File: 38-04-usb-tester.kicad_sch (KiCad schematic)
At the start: 64 parts, among them J1 Conn_1x05, J2 USB_C_12401832E402A, J3 USB_C_12401832E402A, J4 USB_Micro-B_KH-MICRO5P-JN, J5 USB_Mini-B_U-M-M5DD-W-1, J6 USB3_A_HC-USB3.0-L168-WP, SW1 SW_DPDT_x2, SW2 ZX-1.27BM-4PSMD, U1 STM32C031K6Tx

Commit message: edited schematic, added solder mask expansion, added more thermal reliefs
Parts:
- BT1, C3, C5, J1, R1, R2, R3, R4, R5, SW1: LCSC Part # (none) -> DNP; now not fitted
- C1, C2, C4: LCSC Part # (none) -> C527030
- D1, D10, D11, D12, D13, D14, D15, D16, D17, D18, D19, D2, D20, D21, D22, D23, D24, D25, D3, D4, D5, D6, D7, D8, D9: LCSC Part # (none) -> C91839
- H1, H10, H11, H12, H2, H3, H4, H5, H6, H7, H8, H9: LCSC Part # (none) -> DNP
- J2, J3: LCSC Part # (none) -> C464604
- J4: LCSC Part # (none) -> C962222
- J5: LCSC Part # (none) -> C145778
- J6: LCSC Part # (none) -> C7501850
- RN1, RN2, RN3, RN4, RN5, RN6, RN7: LCSC Part # (none) -> C136833
- SW2: LCSC Part # (none) -> C5160896
- U1: value STM32C031K6Tx -> STM32C031K6T6; JLPCB_MPN (none) -> STM32C031K6T6; JLPCB_Mfg (none) -> STMicroelectronics; JLPCB_Part_No (none) -> C5456169; JLPCB_Price (none) -> $1.2900; JLPCB_URL (none) -> https://jlcpcb.com/partdetail/Stmicroelectronics-STM32C031K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; LCSC Part # (none) -> C5456169

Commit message: rev 1 sent for prod
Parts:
- C1, C2, C4: Basic/Extended (none) -> B; JLPCB_MPN CC0402MRY5V6BB104 -> CL05B104KO5NNNC; JLPCB_Mfg YAGEO -> Samsung Electro-Mechanics; JLPCB_Part_No C527030 -> C1525; JLPCB_Price $0.0016 -> $0.0009; JLPCB_URL (none) -> https://jlcpcb.com/partdetail/1877-CL05B104KO5NNNC/C1525; LCSC Part # C527030 -> C1525
- C3: Basic/Extended (none) -> B; JLPCB_MPN DNP -> CL21A475KAQNNNE; JLPCB_Mfg DNP -> Samsung Electro-Mechanics; JLPCB_Part_No DNP -> C1779; JLPCB_Price DNP -> $0.0110; JLPCB_URL (none) -> https://jlcpcb.com/parts/2nd/Capacitors/Multilayer_Ceramic_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; LCSC Part # DNP -> C1779; now fitted
- C5: Basic/Extended (none) -> B; JLPCB_MPN DNP -> CL21B105KBFNNNE; JLPCB_Mfg DNP -> Samsung Electro-Mechanics; JLPCB_Part_No DNP -> C28323; JLPCB_Price DNP -> $0.0083; JLPCB_URL (none) -> https://jlcpcb.com/partdetail/29074-CL21B105KBFNNNE/C28323; LCSC Part # DNP -> C28323; now fitted
- D1, D10, D11, D12, D13, D14, D15, D16, D17, D18, D19, D2, D20, D21, D22, D23, D24, D25, D3, D4, D5, D6, D7, D8, D9: Basic/Extended (none) -> B; JLPCB_MPN 17-21UYC/S530-A3/TR8 -> KT-0805Y; JLPCB_Mfg Everlight Elec -> Hubei KENTO Elec; JLPCB_Part_No C91839 -> C2296; JLPCB_Price $0.0218 -> $0.0114; JLPCB_URL https://jlcpcb.com/parts/2nd/Optocoupler_LED_Digital_Tube_P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 -> https://jlcpcb.com/partdetail/Hubei_KentoElec-KT0805Y/C2296; LCSC Part # C91839 -> C2296
- J2, J3, J4, J5, J6: Basic/Extended (none) -> E
- R1, R2, R3: Basic/Extended (none) -> B; JLPCB_MPN DNP -> 0805W8F1002T5E; JLPCB_Mfg DNP -> UNI-ROYAL(Uniroyal Elec); JLPCB_Part_No DNP -> C17414; JLPCB_Price DNP -> (none); JLPCB_URL (none) -> https://jlcpcb.com/partdetail/18102-0805W8F1002T5E/C17414; LCSC Part # DNP -> C17414; now fitted
- R4: value 1K -> 2K; Basic/Extended (none) -> B; JLPCB_MPN DNP -> 0805W8F2001T5E; JLPCB_Mfg DNP -> UNI-ROYAL(Uniroyal Elec); JLPCB_Part_No DNP -> C17604; JLPCB_Price DNP -> (none); JLPCB_URL (none) -> https://jlcpcb.com/partdetail/18292-0805W8F2001T5E/C17604; LCSC Part # DNP -> C17604; now fitted
- R5: Basic/Extended (none) -> B; JLPCB_MPN DNP -> 0805W8F2001T5E; JLPCB_Mfg DNP -> UNI-ROYAL(Uniroyal Elec); JLPCB_Part_No DNP -> C17604; JLPCB_Price DNP -> (none); JLPCB_URL (none) -> https://jlcpcb.com/partdetail/18292-0805W8F2001T5E/C17604; LCSC Part # DNP -> C17604; now fitted
- RN1, RN2, RN3, RN4, RN5, RN6, RN7: value 1K -> 1K6; Basic/Extended (none) -> E; JLPCB_MPN YC164-JR-071K1L -> YC124-FR-071K6L; JLPCB_Part_No C136833 -> C728711; JLPCB_Price $0.007 -> $0.0024; LCSC Part # C136833 -> C728711
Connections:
- no-connect marks 18 -> 19

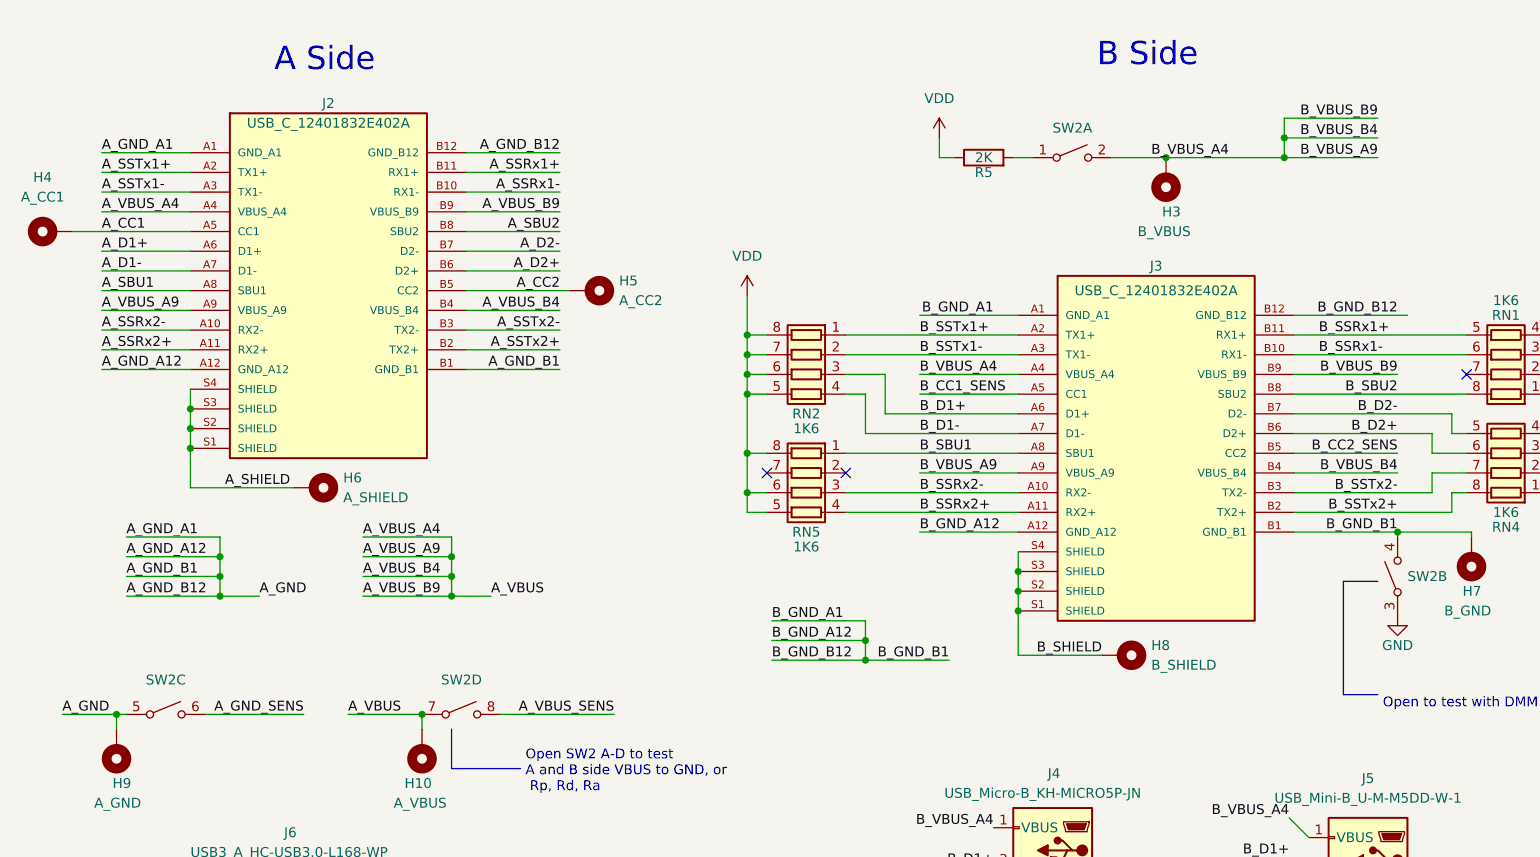
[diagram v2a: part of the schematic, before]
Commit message: correct SW2 footprint and symbol pin numbering
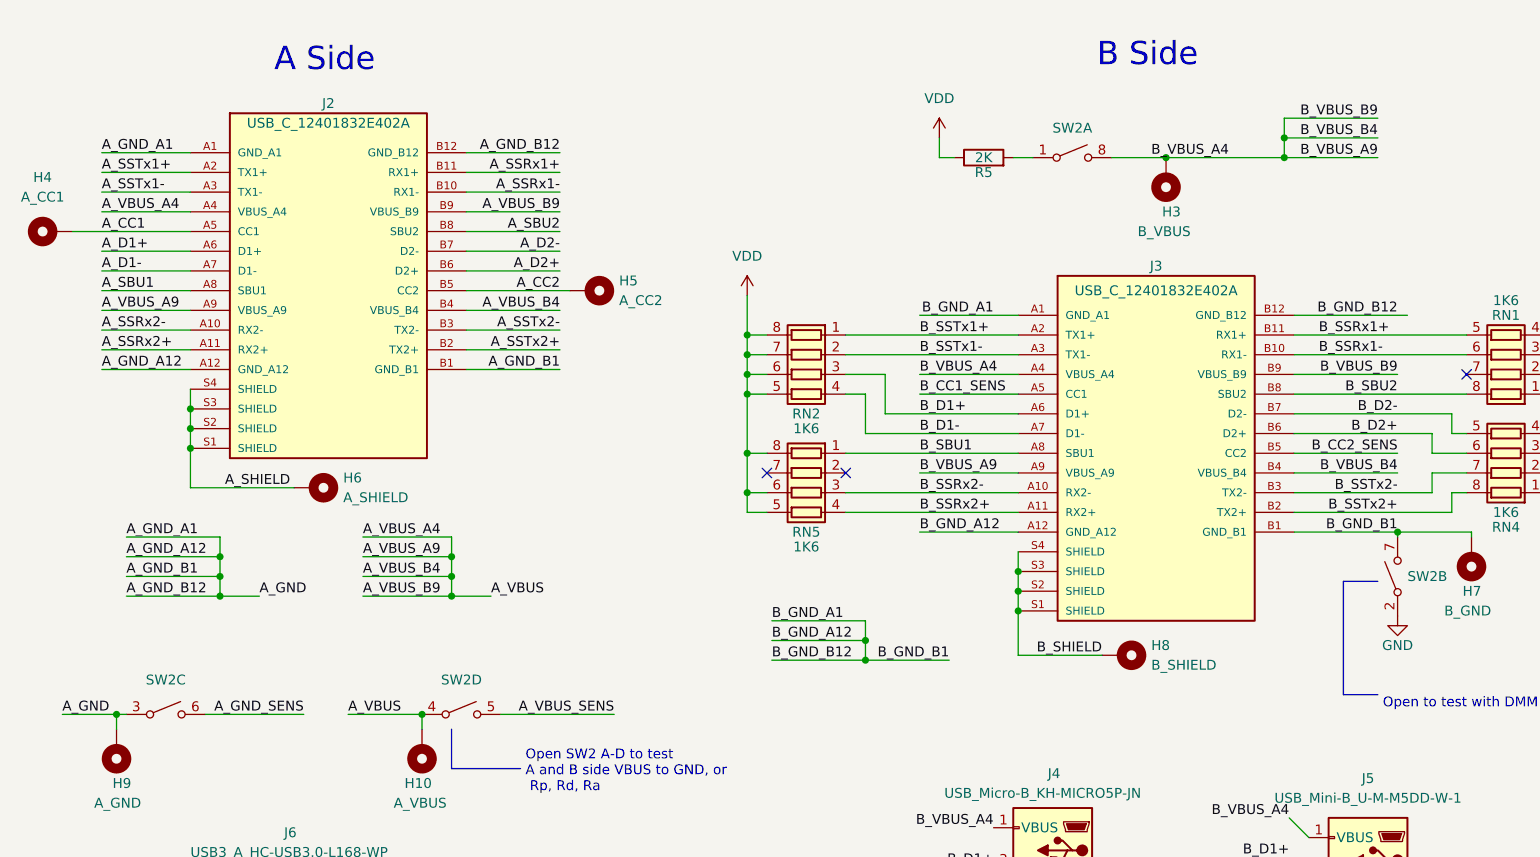
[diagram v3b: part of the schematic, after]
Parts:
- SW2: symbol 01B-UserSchematics:SW_DIP_x04_Separated -> 02-UserSymbols:SW_DIP_x04_Separated
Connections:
- net A_GND: now also SW2.3; no longer SW2.5
- net A_VBUS: now also SW2.4; no longer SW2.7
- net A_VBUS_SENS: now also SW2.5; no longer SW2.8
- net B_GND_A1: now also SW2.7; no longer SW2.4
- net B_VBUS_A4: now also SW2.8; no longer SW2.2
- net GND: now also SW2.2; no longer SW2.3
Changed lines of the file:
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@@
     )
   )
-  (symbol (lib_id "01B-UserSchematics:SW_DIP_x04_Separated") (at 196.85 163.195 90) (unit 2)
+  (symbol (lib_id "02-UserSymbols:SW_DIP_x04_Separated") (at 196.85 163.195 90) (unit 2)
     (in_bom yes) (on_board yes) (dnp no)
     (property "Reference" "SW2" (at 198.12 163.195 90)
@@
     )
   )
-  (symbol (lib_id "01B-UserSchematics:SW_DIP_x04_Separated") (at 76.2 180.975 0) (unit 4)
+  (symbol (lib_id "02-UserSymbols:SW_DIP_x04_Separated") (at 76.2 180.975 0) (unit 4)
     (in_bom yes) (on_board yes) (dnp no) (fields_autoplaced)
     (property "Reference" "SW2" (at 76.2 176.53 0)
@@
     )
   )
-  (symbol (lib_id "01B-UserSchematics:SW_DIP_x04_Separated") (at 154.94 109.22 0) (unit 1)
+  (symbol (lib_id "02-UserSymbols:SW_DIP_x04_Separated") (at 154.94 109.22 0) (unit 1)
     (in_bom yes) (on_board yes) (dnp no) (fields_autoplaced)
     (property "Reference" "SW2" (at 154.94 105.41 0)
@@
     )
   )
-  (symbol (lib_id "01B-UserSchematics:SW_DIP_x04_Separated") (at 38.1 180.975 0) (unit 3)
+  (symbol (lib_id "02-UserSymbols:SW_DIP_x04_Separated") (at 38.1 180.975 0) (unit 3)
     (in_bom yes) (on_board yes) (dnp no) (fields_autoplaced)
     (property "Reference" "SW2" (at 38.1 176.53 0)
